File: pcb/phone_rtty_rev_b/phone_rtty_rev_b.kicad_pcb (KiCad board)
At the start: 2 copper layers, 50 x 50 mm, 38 parts, among them J1 Phone, J2 Transceiver, P1 TRX Data, Q1 2N2222, Q2 2N2222, SW1 1200/9600

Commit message: Minor changes.
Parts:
- moved J2 0.90 mm to (126.0, 59.2)
- moved J1 0.90 mm to (121.0, 90.8)
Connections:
- J1 pad 5: (no net) -> Net-(J1-Pad5)
- J2 pad 5: (no net) -> Net-(J2-Pad5)
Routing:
- net /TRX_DATA_IN: track 39.1 -> 40.9 mm
- net Net-(R11-Pad1): track 11.7 -> 13.2 mm
- net /PTT: track 30.5 -> 31.6 mm
- net /TRX_9600: track 29.4 -> 30.2 mm
- net /TRX_DATA_OUT: track 27.8 -> 28.4 mm
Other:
- board text removed: "RX Gain"

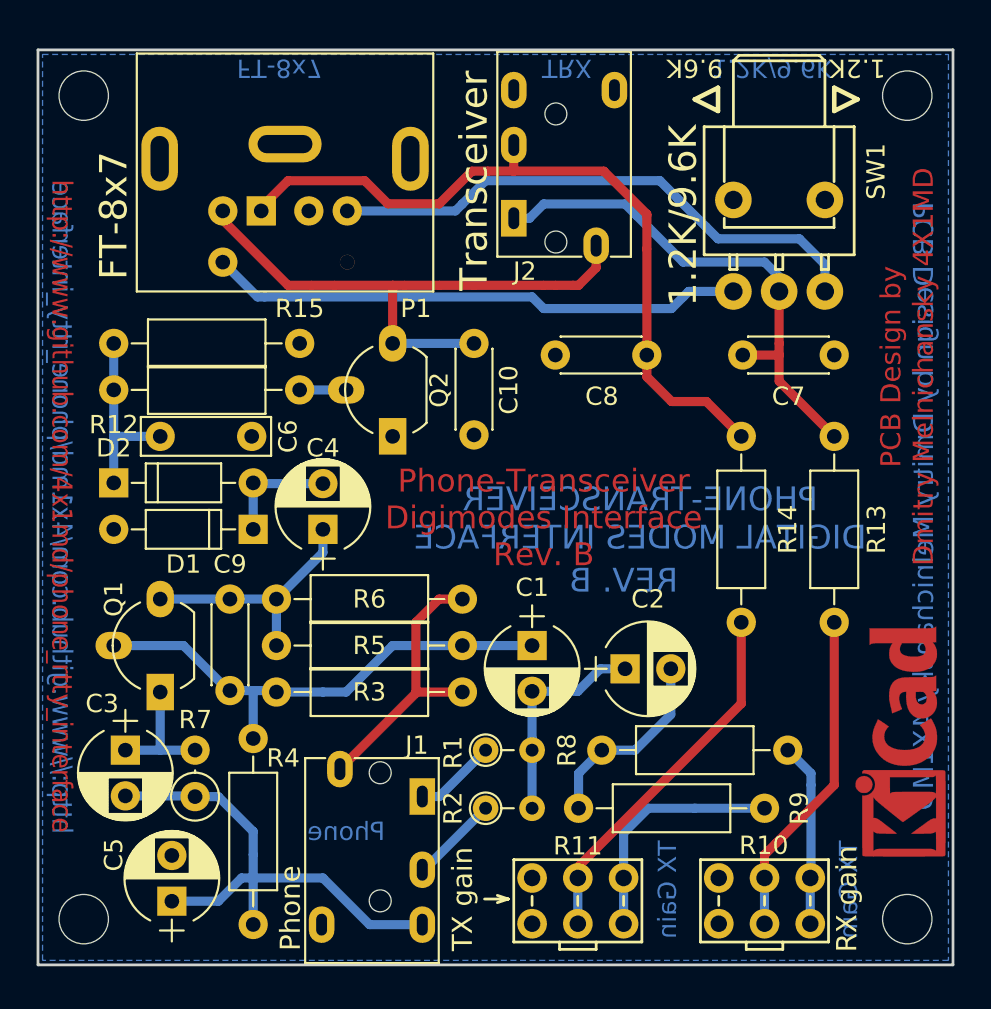
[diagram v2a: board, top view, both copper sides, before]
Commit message: Main board and panels corrections.
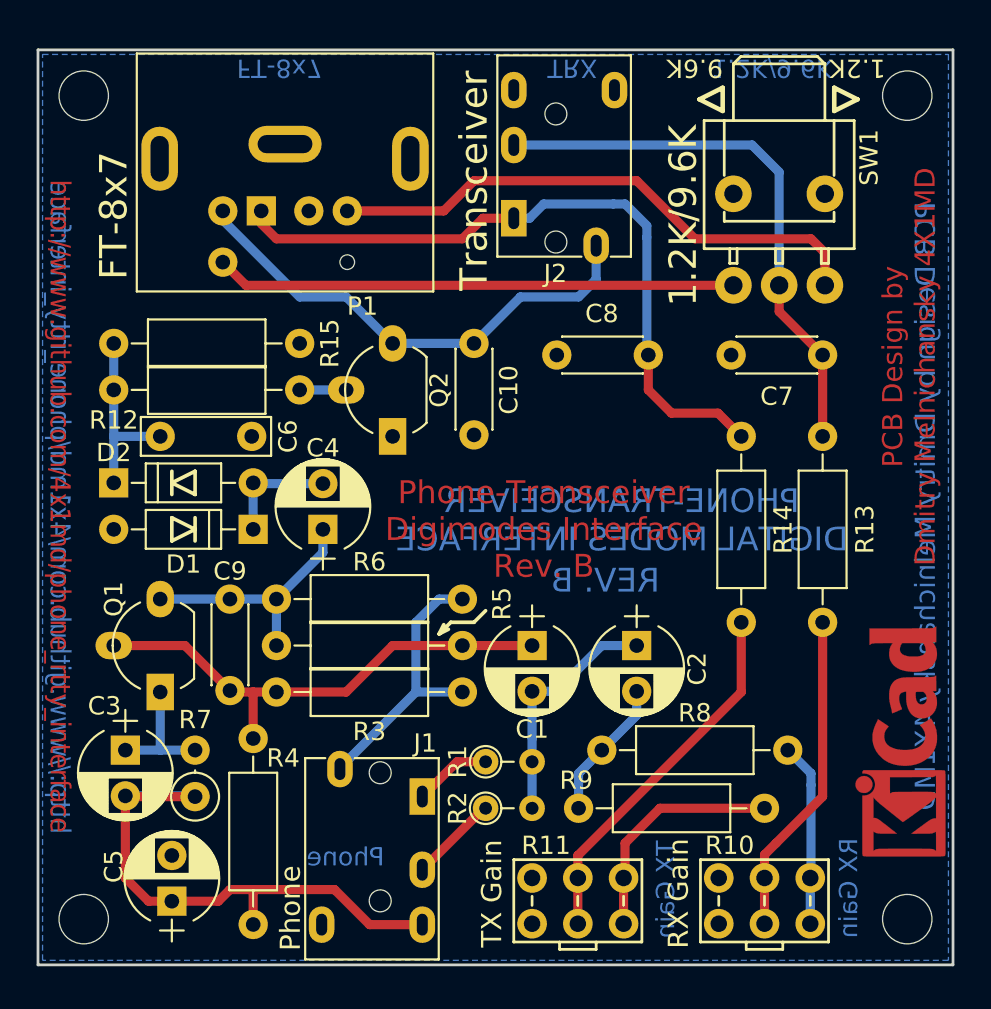
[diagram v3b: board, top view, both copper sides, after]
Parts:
- J1, J2: footprint custom_kicad_footprints:PJ320E_Headphones_Plug_Short -> Phone_RTTY_Footprints:PJ320E_3.5mm_Jack
- P1: footprint custom_kicad_footprints:Connector_Mini-DIN_Female_6Pin_2rows -> Phone_RTTY_Footprints:Connector_Mini-DIN_Female_6Pin_2rows
- R10, R11: footprint custom_kicad_footprints:Potentiometer_Trimmer_Vertical_Multi_Compatible -> Phone_RTTY_Footprints:Potentiometer_Trimmer_Vertical_Multi_Compatible
- SW1: footprint custom_kicad_footprints:Cliff_UT1x_SPDT_ON-ON_Switch_Short -> Phone_RTTY_Footprints:Cliff_UT1x_SPDT_ON-ON_Switch_Short
- moved R14 10.2 mm to (138.4, 71.1), turned to 270 degrees
- moved C8 5.08 mm to (133.3, 66.7), turned to 180 degrees
- moved C2 1.42 mm to (132.7, 82.5), turned to 270 degrees
- moved R2 0.64 mm to (124.5, 88.9)
- moved C7 0.63 mm to (142.9, 66.7)
- moved R13 0.63 mm to (142.9, 71.1)
- moved SW1 0.34 mm to (138.0, 62.9)
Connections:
- C7 pad 1: GNDREF -> /TRX_DATA_OUT
- C7 pad 2: /TRX_DATA_OUT -> GNDREF
- C8 pad 1: GNDREF -> /TRX_DATA_IN
- C8 pad 2: /TRX_DATA_IN -> GNDREF
- J2 pad 1: /TRX_DATA_OUT -> /TRX_DATA_IN
- J2 pad 2: /TRX_DATA_IN -> /TRX_DATA_OUT
- R14 pad 1: Net-(R11-Pad2) -> /TRX_DATA_IN
- R14 pad 2: /TRX_DATA_IN -> Net-(R11-Pad2)
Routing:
- net /PTT: track 31.6 -> 27.0 mm
- net Net-(C2-Pad2): track 11.5 -> 7.71 mm
- net /PHONE_GND: track 28.1 -> 31.7 mm
- net /TRX_DATA_IN: track 40.9 -> 38.7 mm
- net /TRX_DATA_OUT: track 28.4 -> 30.5 mm
- net /PHONE_OUT: track 12.0 -> 13.2 mm
- net /TRX_1200: track 29.3 -> 28.4 mm
- net Net-(R11-Pad2): track 20.2 -> 20.8 mm
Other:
- board text added: "RX Gain"
- board text removed: "RX gain"
- board text removed: "TX gain"
